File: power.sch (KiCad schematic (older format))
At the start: 32 parts, among them U1 MCP1603L, U2 MCP16311/2, U3 MCP16311/2

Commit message: beta
beta pcb version 0.001V
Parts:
- removed C5: 1uF, Capacitors_SMD:C_0402, symbol C
- removed C7: 100nF, Capacitors_SMD:C_0402, symbol C
- removed U3: MCP16311/2, Housings_SSOP:MSOP-8-1EP_3x3mm_Pitch0.65mm, symbol MCP16311/2-RESCUE-autonomous_rc_pcb
- added C105, C106: 22uF, Capacitors_SMD:C_0805_HandSoldering, symbol C
- added C5: 100uF, Capacitor_THT:CP_Radial_D8.0mm_P3.50mm, symbol CP
- added C7: 1000uF, Capacitor_THT:CP_Radial_D8.0mm_P5.00mm, symbol CP
- added D8: 1N5822, PAUL-DIODE-SMD:D_DO-201AD_P5.08mm_Vertical_AnodeUp, symbol Schottky
- added L29: 4.7uH, Inductors_SMD:L_Taiyo-Yuden_NR-50xx_HandSoldering, symbol INDUCTOR
- added R44: 10k, Resistor_SMD:R_0402_1005Metric, symbol R
- added U16: AP3512E, Package_SO:PowerIntegrations_SO-8, symbol AP3512E
- added U3: LM2576S-12/NOPB, Package_TO_SOT_SMD:TO-263-5_TabPin3, symbol LM2576S-12/NOPB
- C1: value 10uF50V -> 10nF
- C10: footprint Capacitors_SMD:C_0402 -> Capacitors_SMD:C_0805_HandSoldering
- C11, C2: value 10uF50V -> 10uF
- C12: value 10uF50V -> 10uF; footprint Capacitors_SMD:C_0402 -> Capacitors_SMD:C_0805_HandSoldering
- C14: value 10uF -> 3.3nF
- L3: value 15uH -> 100uH; footprint Inductors_SMD:L_Abracon_ASPI-3012S -> Inductors_SMD:L_Vishay_IHLP-4040; MPN VLCF4020T-150MR68 -> MSS1210-104KED
- R3: value 31.6k -> 26.1k; footprint Resistors_SMD:R_0402 -> Resistor_SMD:R_0402_1005Metric
- R4: footprint Resistors_SMD:R_0402 -> Resistor_SMD:R_0402_1005Metric
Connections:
- net +3V3: now also C105.1, C106.1, L29.1; no longer C10.1, C14.1, L3.2
- net GND: now also C105.2, C106.2, C5.2, C7.2, D8.A, R44.2, U16.4 (GND), U3.3 (GND), U3.5 (EN); no longer C1.2, C14.2
- net at L3.1: now also D8.K, U3.2 (OUT)
- net at R3.2, R4.1: now also U16.5 (FB)
- net +28V renamed +12V
- net +12V: now also C10.1, L3.2, C7.1, U16.2 (IN), U16.7 (EN), U3.4 (FB); no longer C1.1, R22.1
- new net: C1.1, U16.1 (BS)
- new net: C1.2, L29.2, U16.3 (SW)
- new net: C14.1, U16.6 (COMP)
- new net: C14.2, R44.1
- new net +36V: C5.1, R22.1, U3.1 (V_IN)
- no-connect marks 0 -> 1
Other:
- note added: "1A\n"
- note added: "2A\n"
- note added: "3A\n"
- note added: "40V TO 4V \n"
- note removed: "4.5V to 30V\n"
- moved on the sheet: C1, C11, C13, C2, C3, C4, C6, C8, C9, D5, D6, D7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

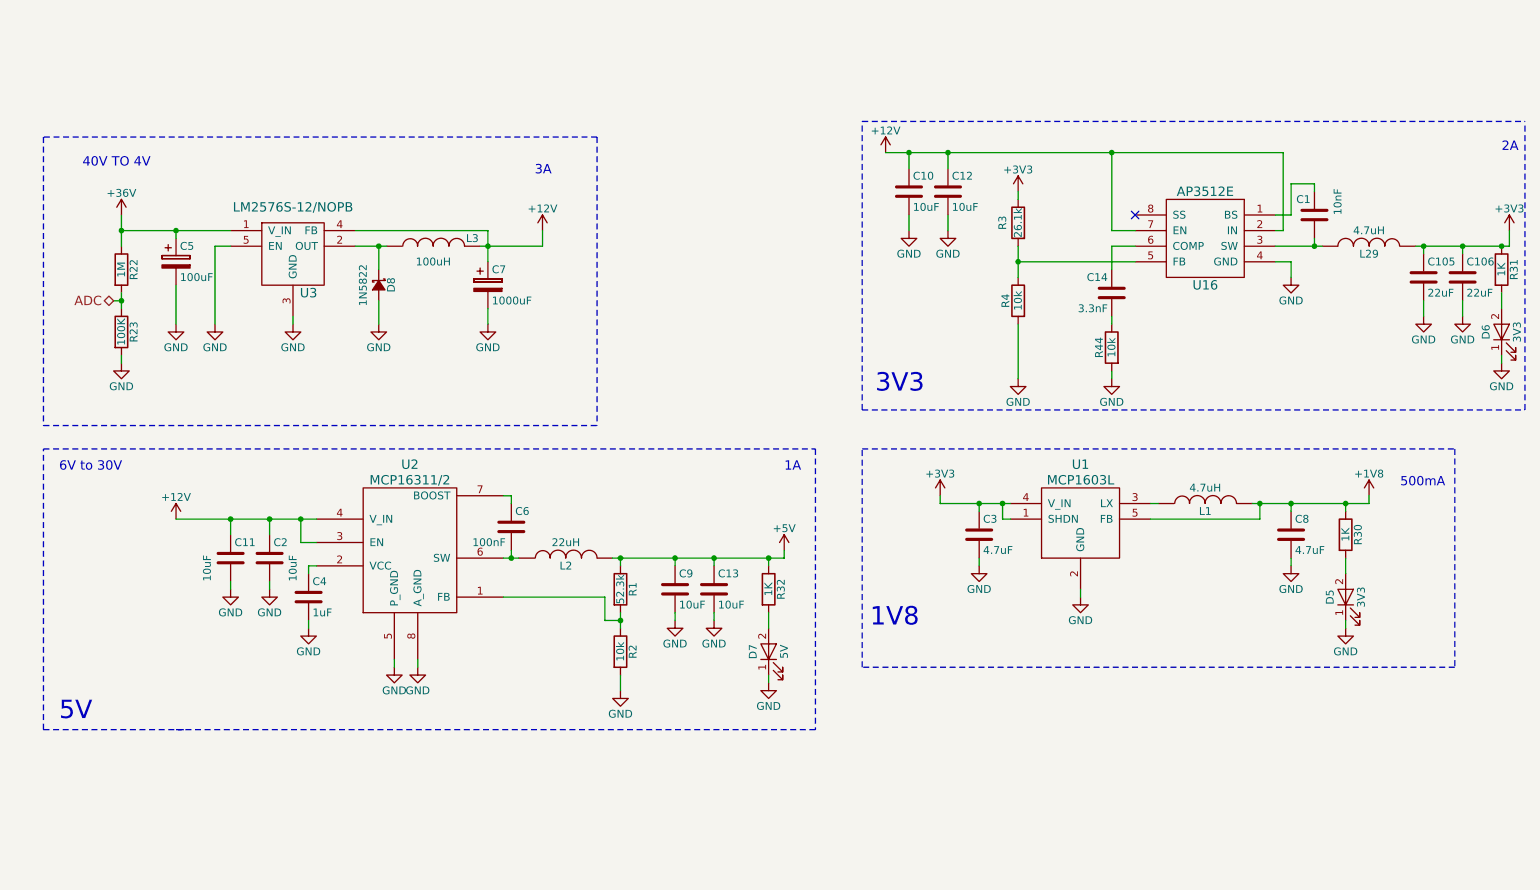
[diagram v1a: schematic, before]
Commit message: tuned rf
added u.fl connectors to tune line 
moved some lines under rf components
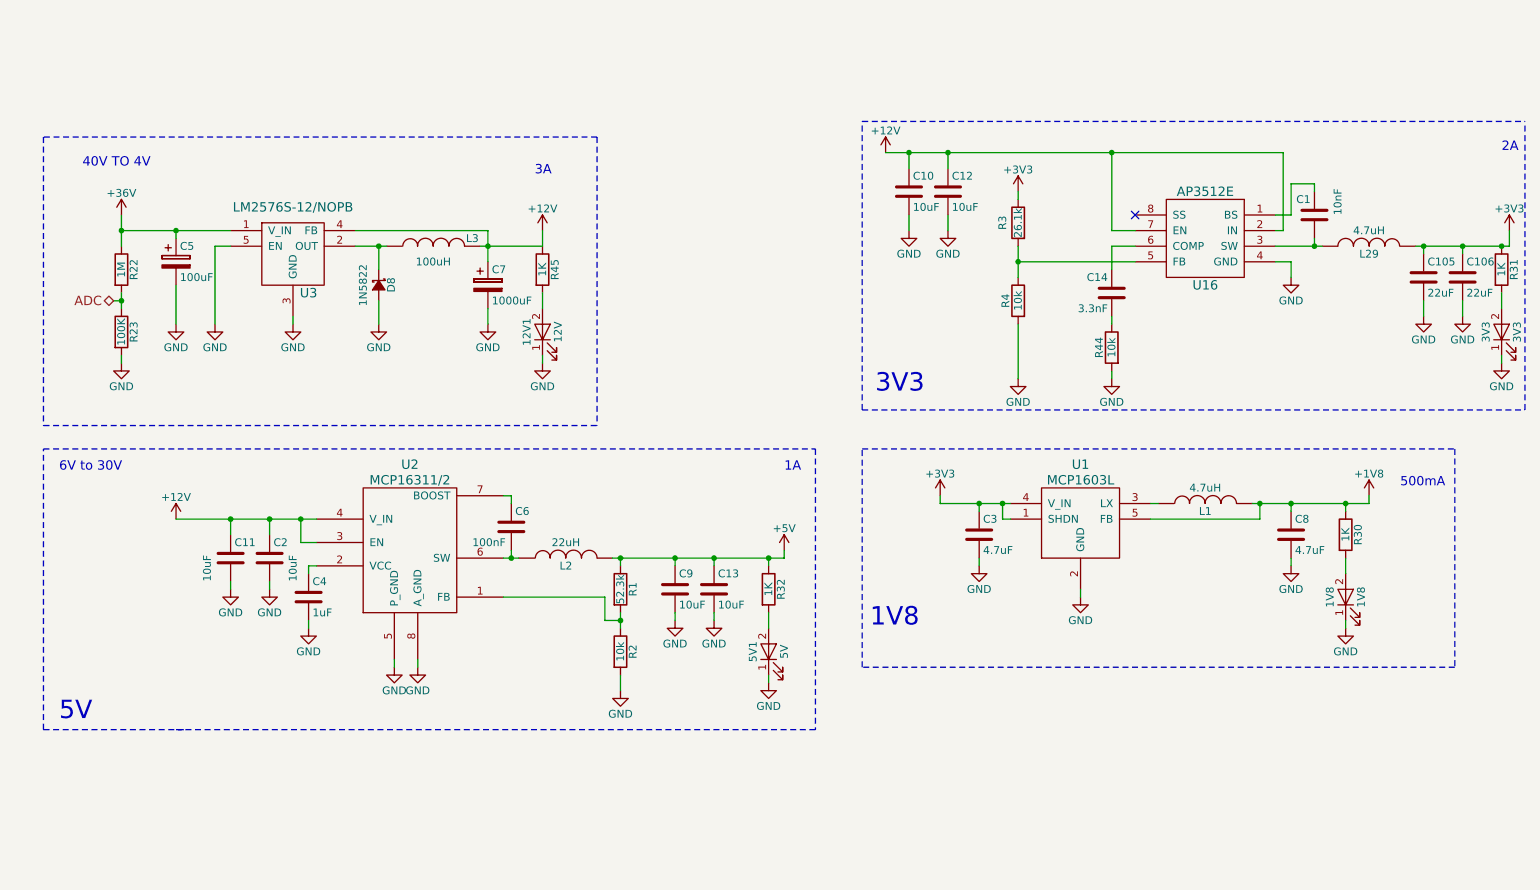
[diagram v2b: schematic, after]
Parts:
- added 12V1: 12V, LEDs:LED_0603, symbol LED
- added R45: 1K, Resistors_SMD:R_0402, symbol R
- 1V8: renamed from D5; value 3V3 -> 1V8
- renumbered D6 to 3V3, D7 to 5V1
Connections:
- net +12V: now also R45.1
- net GND: now also 12V1.1 (K)
- new net: 12V1.2 (A), R45.2
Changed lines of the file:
@@
 $EndComp
 $Comp
-L LED D7
+L LED 5V1
 U 1 1 5AFE29E1
 P 6050 5150
-F 0 "D7" H 6050 5250 50  0000 C CNN
+F 0 "5V1" H 6050 5250 50  0000 C CNN
 F 1 "5V" H 6050 5050 50  0000 C CNN
 F 2 "LEDs:LED_0603" H 6050 5150 50  0001 C CNN
@@
 	6050 4900 6050 5000
 $Comp
-L LED D6
+L LED 3V3
 U 1 1 5AFE541A
 P 10750 3100
-F 0 "D6" H 10750 3200 50  0000 C CNN
+F 0 "3V3" H 10750 3200 50  0000 C CNN
 F 1 "3V3" H 10750 3000 50  0000 C CNN
 F 2 "LEDs:LED_0603" H 10750 3100 50  0001 C CNN
@@
 	10750 2850 10750 2950
 $Comp
-L LED D5
+L LED 1V8
 U 1 1 5AFE571E
 P 9750 4800
-F 0 "D5" H 9750 4900 50  0000 C CNN
-F 1 "3V3" H 9750 4700 50  0000 C CNN
+F 0 "1V8" H 9750 4900 50  0000 C CNN
+F 1 "1V8" H 9750 4700 50  0000 C CNN
 F 2 "LEDs:LED_0603" H 9750 4800 50  0001 C CNN
 F 3 "" H 9750 4800 50  0001 C CNN
@@
 	0    1    1    0
 $EndComp
+$Comp
+L LED 12V1
+U 1 1 5B08A380
+P 4600 3100
+F 0 "12V1" H 4600 3200 50  0000 C CNN
+F 1 "12V" H 4600 3000 50  0000 C CNN
+F 2 "LEDs:LED_0603" H 4600 3100 50  0001 C CNN
+F 3 "" H 4600 3100 50  0001 C CNN
+	1    4600 3100
+	0    -1   -1   0
+$EndComp
+$Comp
+L R R45
+U 1 1 5B08A386
+P 4600 2700
+F 0 "R45" V 4680 2700 50  0000 C CNN
+F 1 "1K" V 4600 2700 50  0000 C CNN
+F 2 "Resistors_SMD:R_0402" V 4530 2700 50  0001 C CNN
+F 3 "" H 4600 2700 50  0001 C CNN
+	1    4600 2700
+	1    0    0    -1
+$EndComp
+$Comp
+L GND #PWR078
+U 1 1 5B08A38C
+P 4600 3300
+F 0 "#PWR078" H 4600 3050 50  0001 C CNN
+F 1 "GND" H 4600 3150 50  0000 C CNN
+F 2 "" H 4600 3300 50  0001 C CNN
+F 3 "" H 4600 3300 50  0001 C CNN
+	1    4600 3300
+	1    0    0    -1
+$EndComp
+Wire Wire Line
+	4600 3300 4600 3250
+Wire Wire Line
+	4600 2850 4600 2950
 $EndSCHEMATC
